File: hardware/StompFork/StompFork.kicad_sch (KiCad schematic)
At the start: 32 parts, among them J1 Line-Level Input, J2 Direct Output, J3 Stompbox Output 1, J4 Stompbox Output 2, J5 Power, U1 TL074

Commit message: Update PCB
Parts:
- C1: footprint (none) -> Capacitor_THT:C_Rect_L24.0mm_W7.0mm_P22.50mm_MKT
- C10, C2, C3, C4, C8: footprint (none) -> Capacitor_THT:C_Disc_D5.0mm_W2.5mm_P5.00mm
- C11, C9: footprint (none) -> Capacitor_THT:C_Radial_D6.3mm_H11.0mm_P2.50mm
- C5, C6, C7: footprint (none) -> Capacitor_THT:C_Radial_D10.0mm_H12.5mm_P5.00mm
- J1, J2, J3, J4, J5: footprint (none) -> Connector_JST:JST_EH_B2B-EH-A_1x02_P2.50mm_Vertical
- R1, R2, R3, R4: footprint (none) -> Resistor_THT:R_Axial_DIN0207_L6.3mm_D2.5mm_P2.54mm_Vertical
- R10, R11, R12, R5, R6, R7, R8, R9: footprint (none) -> Resistor_THT:R_Axial_DIN0207_L6.3mm_D2.5mm_P10.16mm_Horizontal
- RV1, RV2: footprint (none) -> Connector_JST:JST_EH_B3B-EH-A_1x03_P2.50mm_Vertical
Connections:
- net GND: now also J1.2 (S), J2.2 (S), J3.2 (S), J4.2 (S); no longer J1.S, J2.S, J3.S, J4.S
- net at C4.1, U1.13 (-): now also R4.2; no longer R4.1
- net at R7.1, U1.14: now also R4.1; no longer R4.2
- net at C2.1, U1.6 (-): now also R2.2; no longer R2.1
- net at R5.1, RV1.1, RV2.1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: now also R2.1; no longer R2.2
- net at C1.2: now also J1.1 (T); no longer J1.T
- net at C3.1, U1.9 (-): now also R3.2; no longer R3.1
- net at R6.1, U1.8: now also R3.1; no longer R3.2
- net at C7.2, R10.2: now also J4.1 (T); no longer J4.T
- net at C6.2, R9.2: now also J3.1 (T); no longer J3.T
- net at C5.2, R8.2: now also J2.1 (T); no longer J2.T
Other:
- moved on the sheet: R2, R3, R4
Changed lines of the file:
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@@
 	(symbol
 		(lib_id "Device:R")
-		(at 196.85 120.65 90)
+		(at 196.85 120.65 270)
+		(mirror x)
 		(unit 1)
 		(exclude_from_sim no)
@@
 			)
 		)
-		(property "Footprint" ""
+		(property "Footprint" "Resistor_THT:R_Axial_DIN0207_L6.3mm_D2.5mm_P2.54mm_Vertical"
 			(at 196.85 122.428 90)
 			(effects
@@
 	(symbol
 		(lib_id "Device:R")
-		(at 88.9 57.15 90)
+		(at 88.9 57.15 270)
+		(mirror x)
 		(unit 1)
 		(exclude_from_sim no)
@@
 			)
 		)
-		(property "Footprint" ""
+		(property "Footprint" "Resistor_THT:R_Axial_DIN0207_L6.3mm_D2.5mm_P2.54mm_Vertical"
 			(at 88.9 58.928 90)
 			(effects
@@
 			)
 		)
-		(property "Footprint" ""
+		(property "Footprint" "Resistor_THT:R_Axial_DIN0207_L6.3mm_D2.5mm_P2.54mm_Vertical"
 			(at 74.422 31.75 90)
 			(effects
@@
 			)
 		)
-		(property "Footprint" ""
+		(property "Footprint" "Capacitor_THT:C_Rect_L24.0mm_W7.0mm_P22.50mm_MKT"
 			(at 46.99 42.8752 0)
 			(effects
@@
 			)
 		)
-		(property "Description" "Electrolytic or Film (MKP/MKT)"
-			(at 53.34 30.734 90)
+		(property "Description" "Electrolytic or Film (PP/PET)"
+			(at 52.324 29.718 90)
 			(effects
 				(font
@@
 	(symbol
 		(lib_id "Device:R")
-		(at 152.4 76.2 90)
+		(at 152.4 76.2 270)
+		(mirror x)
 		(unit 1)
 		(exclude_from_sim no)
@@
 			)
 		)
-		(property "Footprint" ""
+		(property "Footprint" "Resistor_THT:R_Axial_DIN0207_L6.3mm_D2.5mm_P2.54mm_Vertical"
 			(at 152.4 77.978 90)
 			(effects
@@
 			)
 		)
-		(property "Footprint" ""
+		(property "Footprint" "Capacitor_THT:C_Disc_D5.0mm_W2.5mm_P5.00mm"
 			(at 200.66 134.3152 0)
 			(effects
@@
 			)
 		)
-		(property "Footprint" ""
+		(property "Footprint" "Resistor_THT:R_Axial_DIN0207_L6.3mm_D2.5mm_P10.16mm_Horizontal"
 			(at 222.25 46.228 90)
 			(effects
@@
 			)
 		)
-		(property "Footprint" ""
+		(property "Footprint" "Connector_JST:JST_EH_B2B-EH-A_1x02_P2.50mm_Vertical"
 			(at 271.78 118.11 0)
 			(effects
@@
 			)
 		)
-		(pin "T"
+		(pin "2"
 		)
-		(pin "S"
+		(pin "1"
 		)
 		(instances
@@
 			)
 		)
-		(property "Footprint" ""
+		(property "Footprint" "Capacitor_THT:C_Radial_D6.3mm_H11.0mm_P2.50mm"
 			(at 102.5652 118.11 0)
 			(effects
@@
 			)
 		)
-		(property "Footprint" ""
+		(property "Footprint" "Capacitor_THT:C_Radial_D6.3mm_H11.0mm_P2.50mm"
 			(at 64.4652 175.26 0)
 			(effects
@@
 	)
 	(symbol
+		(lib_name "AudioJack2_1")
 		(lib_id "Connector_Audio:AudioJack2")
 		(at 26.67 41.91 0)
@@
 			)
 		)
-		(property "Footprint" ""
+		(property "Footprint" "Connector_JST:JST_EH_B2B-EH-A_1x02_P2.50mm_Vertical"
 			(at 26.67 41.91 0)
 			(effects
@@
 			)
 		)
-		(pin "T"
+		(pin "2"
 		)
-		(pin "S"
+		(pin "1"
 		)
 		(instances
@@
 			)
 		)
-		(property "Footprint" ""
+		(property "Footprint" "Capacitor_THT:C_Disc_D5.0mm_W2.5mm_P5.00mm"
 			(at 45.4152 175.26 0)
 			(effects
@@
 			)
 		)
-		(property "Footprint" ""
+		(property "Footprint" "Capacitor_THT:C_Radial_D10.0mm_H12.5mm_P5.00mm"
 			(at 238.76 106.9848 0)
 			(effects
@@
 			)
 		)
-		(property "Footprint" ""
+		(property "Footprint" "Resistor_THT:R_Axial_DIN0207_L6.3mm_D2.5mm_P10.16mm_Horizontal"
 			(at 222.25 109.728 90)
 			(effects
@@
 			)
 		)
-		(property "Footprint" ""
+		(property "Footprint" "Resistor_THT:R_Axial_DIN0207_L6.3mm_D2.5mm_P10.16mm_Horizontal"
 			(at 249.428 82.55 90)
 			(effects
@@
 			)
 		)
-		(property "Footprint" ""
+		(property "Footprint" "Capacitor_THT:C_Disc_D5.0mm_W2.5mm_P5.00mm"
 			(at 83.5152 118.11 0)
 			(effects
@@
 			)
 		)
-		(property "Footprint" ""
+		(property "Footprint" "Resistor_THT:R_Axial_DIN0207_L6.3mm_D2.5mm_P10.16mm_Horizontal"
 			(at 249.428 114.3 90)
 			(effects
@@
 	)
 	(symbol
+		(lib_name "AudioJack2_3")
 		(lib_id "Connector_Audio:AudioJack2")
 		(at 271.78 86.36 180)
@@
 			)
 		)
-		(property "Footprint" ""
+		(property "Footprint" "Connector_JST:JST_EH_B2B-EH-A_1x02_P2.50mm_Vertical"
 			(at 271.78 86.36 0)
 			(effects
@@
 			)
 		)
-		(pin "T"
+		(pin "2"
 		)
-		(pin "S"
+		(pin "1"
 		)
 		(instances
@@
 			)
 		)
-		(property "Footprint" ""
+		(property "Footprint" "Resistor_THT:R_Axial_DIN0207_L6.3mm_D2.5mm_P10.16mm_Horizontal"
 			(at 29.972 156.21 90)
 			(effects
@@
 		(on_board yes)
 		(dnp no)
-		(fields_autoplaced yes)
 		(property "Reference" "C5"
 			(at 234.061 36.83 90)
@@
 			)
 		)
-		(property "Footprint" ""
+		(property "Footprint" "Capacitor_THT:C_Radial_D10.0mm_H12.5mm_P5.00mm"
 			(at 238.76 43.4848 0)
 			(effects
@@
 			)
 		)
-		(property "Description" "Polarized capacitor"
-			(at 234.95 44.45 0)
+		(property "Description" "Polarized or Bipolar (C5-C7)"
+			(at 238.252 32.258 90)
 			(effects
 				(font
 					(size 1.27 1.27)
 				)
-				(hide yes)
 			)
 		)
@@
 			)
 		)
-		(property "Footprint" ""
+		(property "Footprint" "Connector_JST:JST_EH_B3B-EH-A_1x03_P2.50mm_Vertical"
 			(at 171.45 105.41 0)
 			(effects
@@
 	)
 	(symbol
+		(lib_name "AudioJack2_2")
 		(lib_id "Connector_Audio:AudioJack2")
 		(at 271.78 54.61 180)
@@
 			)
 		)
-		(property "Footprint" ""
+		(property "Footprint" "Connector_JST:JST_EH_B2B-EH-A_1x02_P2.50mm_Vertical"
 			(at 271.78 54.61 0)
 			(effects
@@
 			)
 		)
-		(pin "T"
+		(pin "2"
 		)
-		(pin "S"
+		(pin "1"
 		)
 		(instances
@@
 			)
 		)
-		(property "Footprint" ""
+		(property "Footprint" "Capacitor_THT:C_Disc_D5.0mm_W2.5mm_P5.00mm"
 			(at 156.21 89.8652 0)
 			(effects
@@
 			)
 		)
-		(property "Footprint" ""
+		(property "Footprint" "Connector_JST:JST_EH_B2B-EH-A_1x02_P2.50mm_Vertical"
 			(at 26.67 113.03 0)
 			(effects
@@
 			)
 		)
-		(property "Footprint" ""
+		(property "Footprint" "Capacitor_THT:C_Radial_D10.0mm_H12.5mm_P5.00mm"
 			(at 238.76 75.2348 0)
 			(effects
@@
 			)
 		)
-		(property "Footprint" ""
+		(property "Footprint" "Capacitor_THT:C_Disc_D5.0mm_W2.5mm_P5.00mm"
 			(at 92.71 70.8152 0)
 			(effects
@@
 			)
 		)
-		(property "Footprint" ""
+		(property "Footprint" "Resistor_THT:R_Axial_DIN0207_L6.3mm_D2.5mm_P10.16mm_Horizontal"
 			(at 222.25 77.978 90)
 			(effects
@@
 			)
 		)
-		(property "Footprint" ""
+		(property "Footprint" "Connector_JST:JST_EH_B3B-EH-A_1x03_P2.50mm_Vertical"
 			(at 127 60.96 0)
 			(effects
@@
 			)
 		)
-		(property "Footprint" ""
+		(property "Footprint" "Resistor_THT:R_Axial_DIN0207_L6.3mm_D2.5mm_P10.16mm_Horizontal"
 			(at 29.972 171.45 90)
 			(effects
@@
 			)
 		)
-		(property "Footprint" ""
+		(property "Footprint" "Resistor_THT:R_Axial_DIN0207_L6.3mm_D2.5mm_P10.16mm_Horizontal"
 			(at 249.428 50.8 90)
 			(effects

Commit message: Update PCB
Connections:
- net VREF: now also RV1.1; no longer RV1.3
- net at R2.1, R5.1, RV2.1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: now also RV1.3; no longer RV1.1
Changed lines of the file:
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@@
 		(on_board yes)
 		(dnp no)
-		(fields_autoplaced yes)
 		(property "Reference" "RV2"
 			(at 168.91 104.1399 0)
@@
 		(lib_id "Device:R_Potentiometer")
 		(at 127 60.96 0)
-		(unit 1)
-		(exclude_from_sim no)
-		(in_bom yes)
-		(on_board yes)
-		(dnp no)
-		(fields_autoplaced yes)
+		(mirror x)
+		(unit 1)
+		(exclude_from_sim no)
+		(in_bom yes)
+		(on_board yes)
+		(dnp no)
 		(property "Reference" "RV1"
-			(at 124.46 59.6899 0)
+			(at 124.46 62.2301 0)
 			(effects
 				(font
@@
 		)
 		(property "Value" "10k"
-			(at 124.46 62.2299 0)
-			(effects
-				(font
+			(at 124.46 59.6901 0)
+			(effects
+				(font

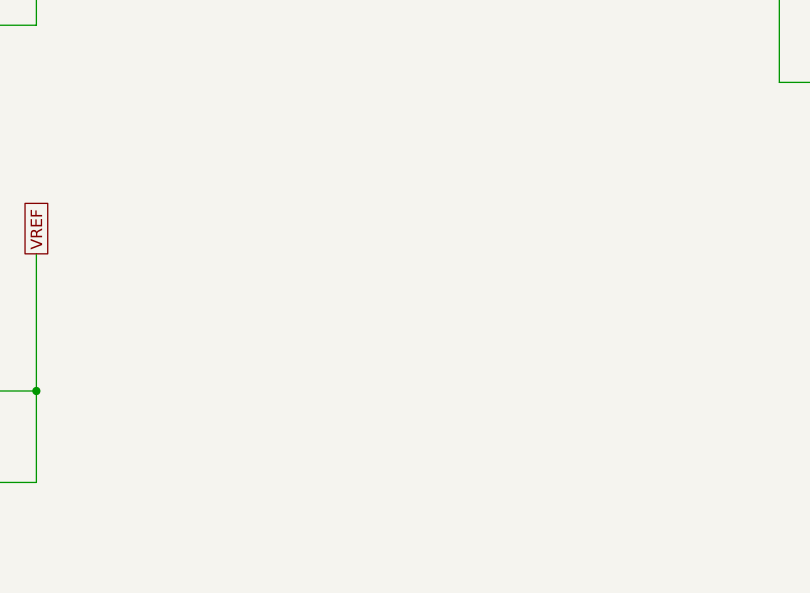
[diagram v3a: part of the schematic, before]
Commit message: Add status LED
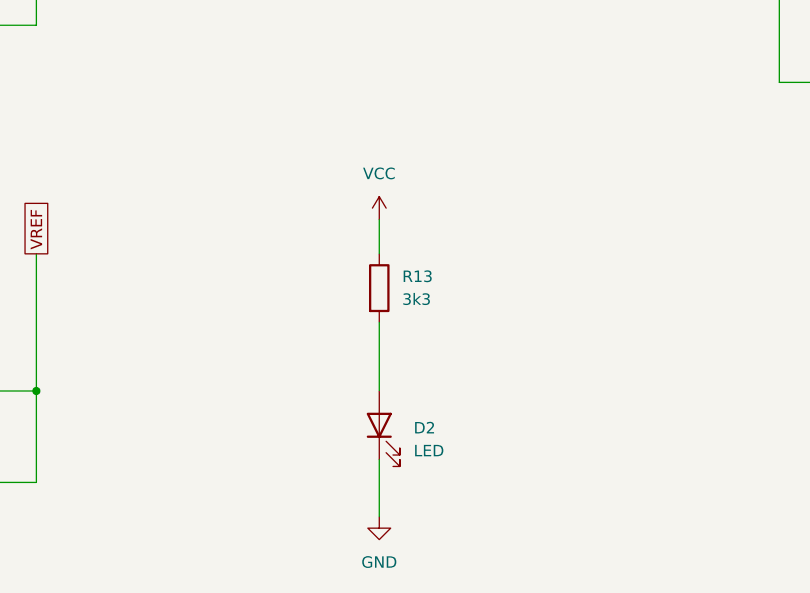
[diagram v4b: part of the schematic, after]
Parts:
- added D2: LED, Connector_JST:JST_EH_B2B-EH-A_1x02_P2.50mm_Vertical, symbol Device:LED
- added R13: 3k3, Resistor_THT:R_Axial_DIN0207_L6.3mm_D2.5mm_P10.16mm_Horizontal, symbol Device:R
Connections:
- net GND: now also D2.1 (K)
- net VCC: now also R13.1
- new net: D2.2 (A), R13.2

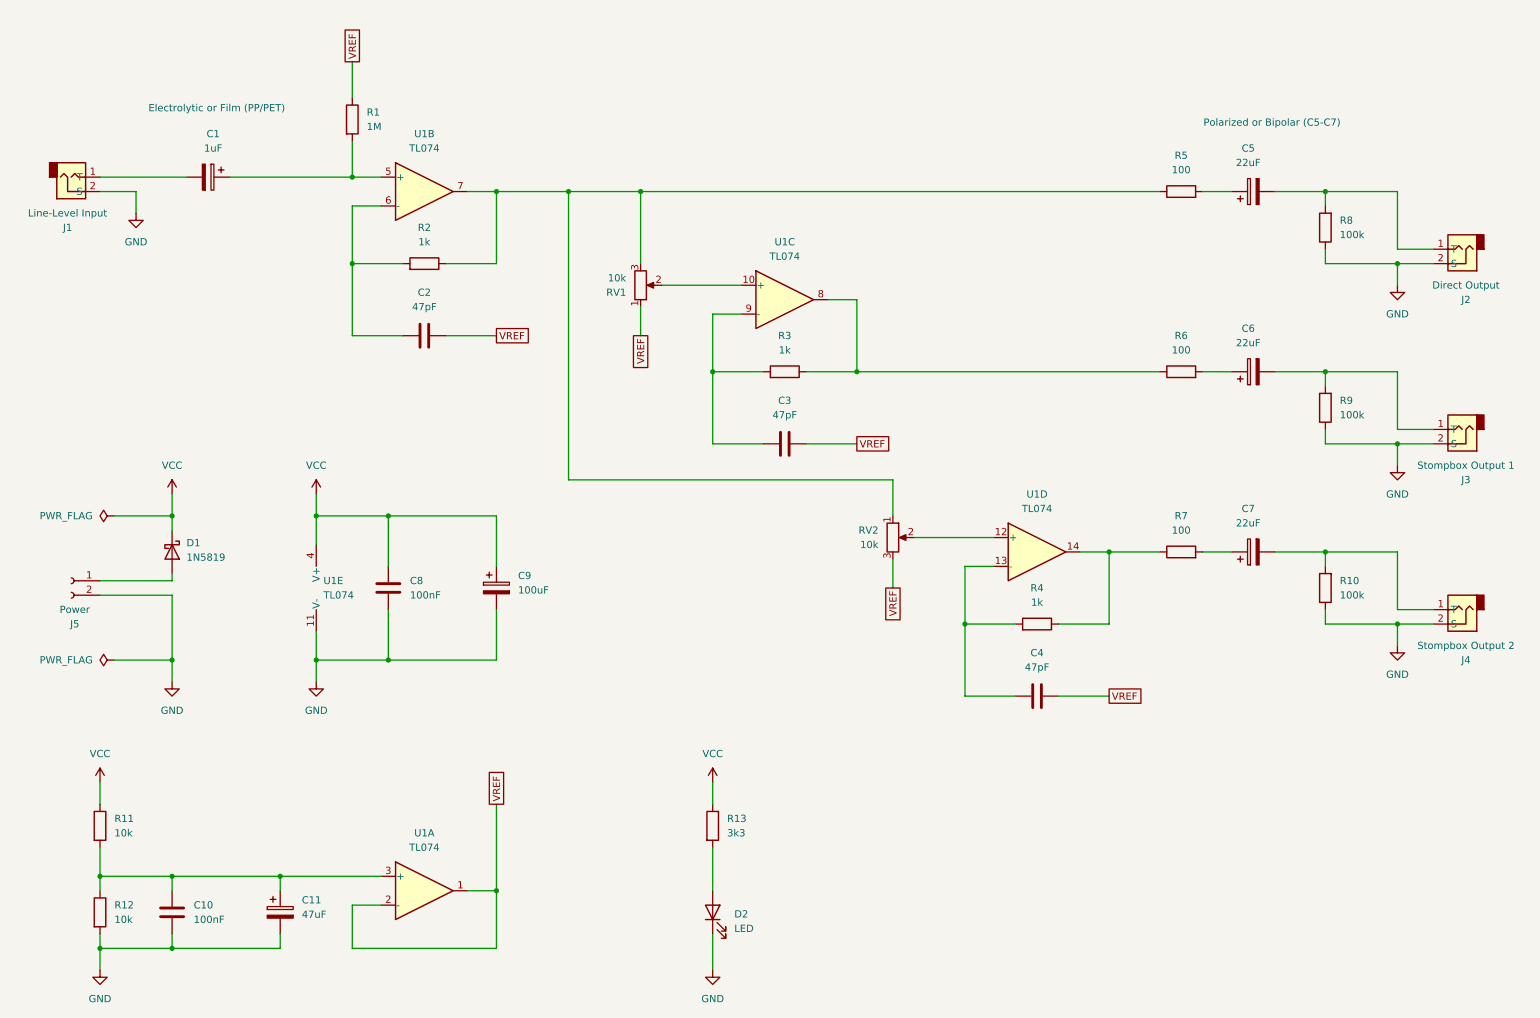
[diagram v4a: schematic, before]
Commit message: Rename VREF to VGND
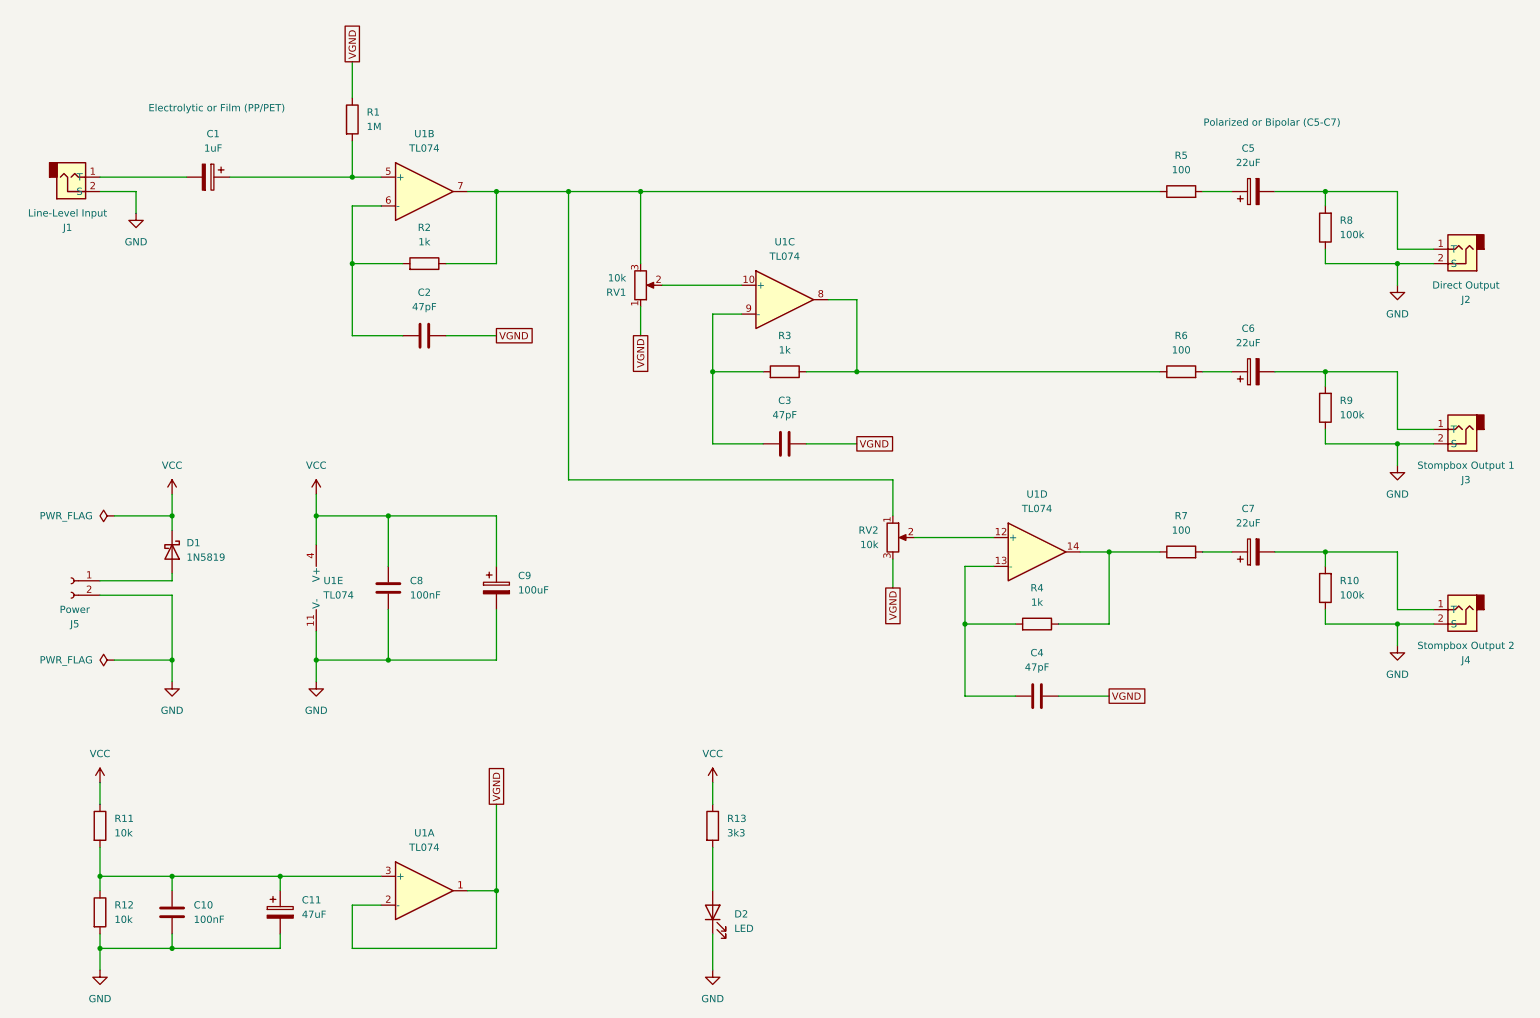
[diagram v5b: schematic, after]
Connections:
- net VREF renamed VGND
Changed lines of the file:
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@@
 		)
 	)
-	(global_label "VREF"
+	(global_label "VGND"
 		(shape passive)
 		(at 209.55 133.35 0)
@@
 		)
 		(property "Intersheetrefs" "${INTERSHEET_REFS}"
-			(at 216.0201 133.35 0)
+			(at 216.383 133.35 0)
 			(effects
 				(font
@@
 		)
 	)
-	(global_label "VREF"
+	(global_label "VGND"
 		(shape passive)
 		(at 165.1 88.9 0)
@@
 		)
 		(property "Intersheetrefs" "${INTERSHEET_REFS}"
-			(at 171.5701 88.9 0)
+			(at 171.933 88.9 0)
 			(effects
 				(font
@@
 		)
 	)
-	(global_label "VREF"
+	(global_label "VGND"
 		(shape passive)
 		(at 76.2 21.59 90)
@@
 		)
 		(property "Intersheetrefs" "${INTERSHEET_REFS}"
-			(at 76.2 15.1199 90)
+			(at 76.2 14.757 90)
 			(effects
 				(font
@@
 		)
 	)
-	(global_label "VREF"
+	(global_label "VGND"
 		(shape passive)
 		(at 171.45 114.3 270)
@@
 		)
 		(property "Intersheetrefs" "${INTERSHEET_REFS}"
-			(at 171.45 120.7701 90)
+			(at 171.45 121.133 90)
 			(effects
 				(font
@@
 		)
 	)
-	(global_label "VREF"
+	(global_label "VGND"
 		(shape passive)
 		(at 101.6 152.4 90)
@@
 		)
 		(property "Intersheetrefs" "${INTERSHEET_REFS}"
-			(at 101.6 145.9299 90)
+			(at 101.6 145.567 90)
 			(effects
 				(font
@@
 		)
 	)
-	(global_label "VREF"
+	(global_label "VGND"
 		(shape passive)
 		(at 101.6 69.85 0)
@@
 		)
 		(property "Intersheetrefs" "${INTERSHEET_REFS}"
-			(at 108.0701 69.85 0)
+			(at 108.433 69.85 0)
 			(effects
 				(font
@@
 		)
 	)
-	(global_label "VREF"
+	(global_label "VGND"
 		(shape passive)
 		(at 127 69.85 270)
@@
 		)
 		(property "Intersheetrefs" "${INTERSHEET_REFS}"
-			(at 127 76.3201 90)
+			(at 127 76.683 90)
 			(effects
 				(font
